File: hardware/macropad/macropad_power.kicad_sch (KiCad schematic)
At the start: 27 parts, among them J1 Conn_01x02, Q1 Q_PMOS, Q2 FS8205A, SW1 SW_SPDT, SW2 SW_SPDT, U1 TP4056-42-ESOP8, U2 DW01A, U3 RT8010AGQW, U4 LP2992IM5-3.3/NOPB

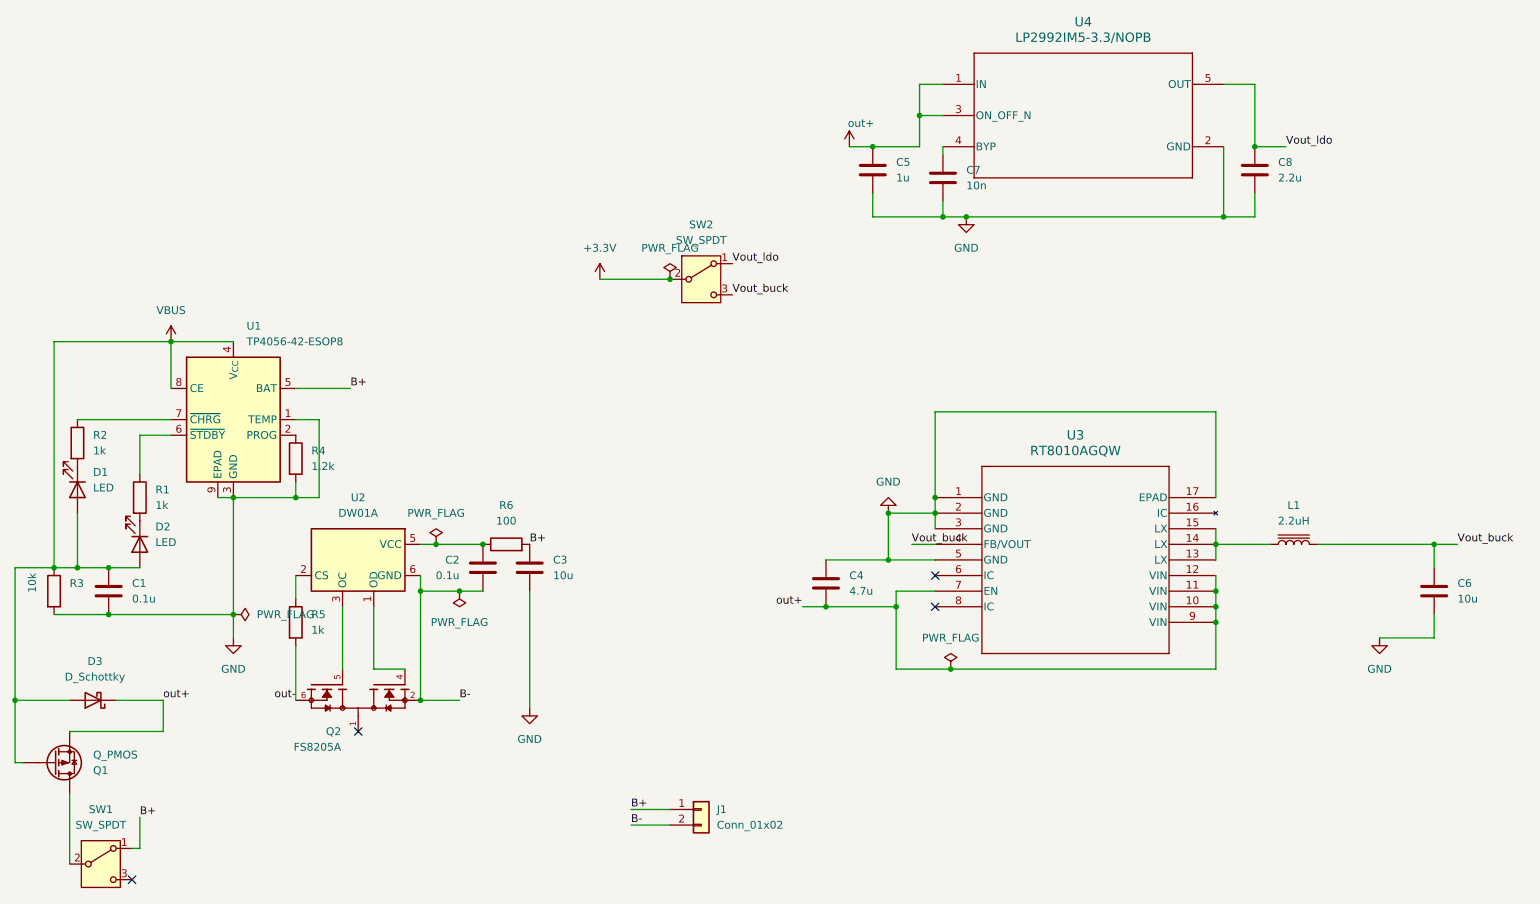
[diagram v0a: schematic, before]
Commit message: pcb macropad done
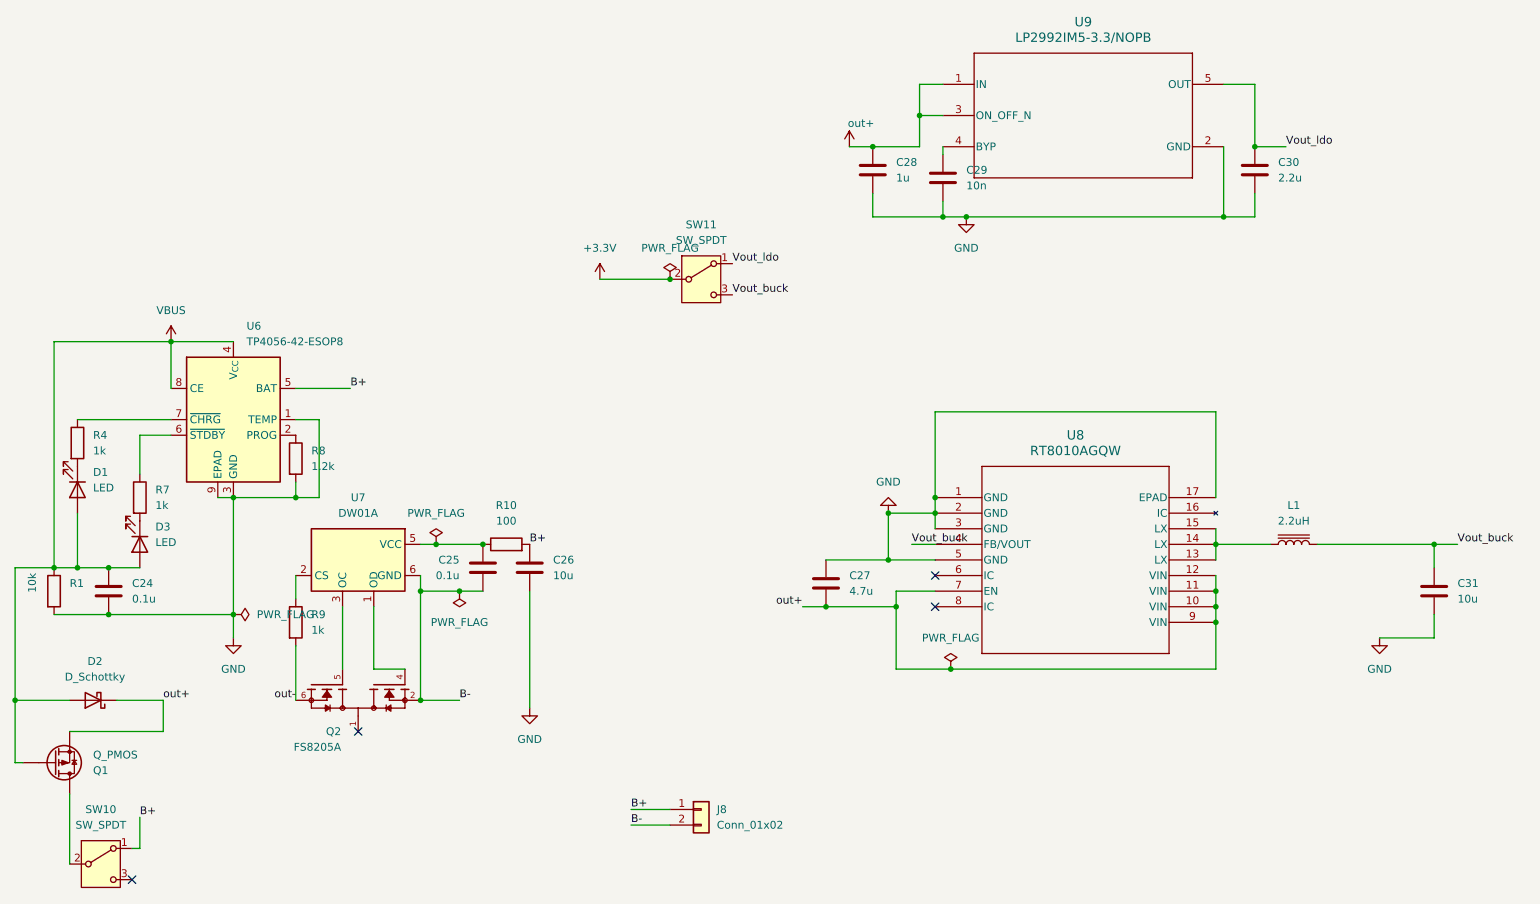
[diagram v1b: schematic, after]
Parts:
- renumbered C1 to C24, C2 to C25, C3 to C26, C4 to C27, C5 to C28, C7 to C29, C8 to C30, C6 to C31, D3 to D2, D2 to D3, J1 to J8, R3 to R1, R6 to R10, R2 to R4, R1 to R7, R4 to R8, R5 to R9, SW1 to SW10, SW2 to SW11, U1 to U6, U2 to U7, U3 to U8, U4 to U9

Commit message: routing
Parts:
- removed SW11: SW_SPDT, SS12F23L5:SS12F23L5 spdt, symbol Switch:SW_SPDT
- added J6: Conn_01x03_Socket, Connector_Hirose:Hirose_DF13-03P-1.25DSA_1x03_P1.25mm_Vertical, symbol Connector:Conn_01x03_Socket
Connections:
- net +3.3V: now also J6.2 (Pin_2)
- net Vout_buck: now also J6.1 (Pin_1)
- net Vout_ldo: now also J6.3 (Pin_3)
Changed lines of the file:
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@@
 	(paper "A3")
 	(junction
-		(at 196.85 86.36)
-		(diameter 0)
-		(color 0 0 0 0)
-	)
-	(junction
 		(at 285.75 129.54)
 		(diameter 0)
@@
 	)
 	(junction
+		(at 185.42 96.52)
+		(diameter 0)
+		(color 0 0 0 0)
+	)
+	(junction
 		(at 285.75 139.7)
 		(diameter 0)
@@
 	(wire
 		(pts
+			(xy 173.99 96.52) (xy 173.99 95.25)
+		)
+		(stroke
+			(width 0)
+			(type default)
+		)
+	)
+	(wire
+		(pts
 			(xy 106.68 154.94) (xy 114.3 154.94)
 		)
@@
 	(wire
 		(pts
+			(xy 185.42 96.52) (xy 185.42 95.25)
+		)
+		(stroke
+			(width 0)
+			(type default)
+		)
+	)
+	(wire
+		(pts
 			(xy 297.18 64.77) (xy 292.1 64.77)
 		)
@@
 	(wire
 		(pts
+			(xy 185.42 96.52) (xy 198.12 96.52)
+		)
+		(stroke
+			(width 0)
+			(type default)
+		)
+	)
+	(wire
+		(pts
 			(xy 156.21 137.16) (xy 156.21 134.62)
 		)
@@
 	(wire
 		(pts
-			(xy 185.42 86.36) (xy 196.85 86.36)
+			(xy 173.99 96.52) (xy 185.42 96.52)
 		)
 		(stroke
@@
 	)
 	(label "Vout_buck"
-		(at 207.01 88.9 0)
+		(at 198.12 93.98 180)
 		(effects
 			(font
 				(size 1.27 1.27)
 			)
-			(justify left bottom)
+			(justify right bottom)
 		)
 	)
@@
 	)
 	(label "Vout_ldo"
-		(at 207.01 83.82 0)
+		(at 198.12 99.06 180)
 		(effects
 			(font
 				(size 1.27 1.27)
 			)
-			(justify left bottom)
+			(justify right bottom)
 		)
 	)
@@
 	(symbol
 		(lib_id "power:PWR_FLAG")
-		(at 196.85 86.36 0)
+		(at 185.42 95.25 0)
 		(unit 1)
 		(exclude_from_sim no)
@@
 		(fields_autoplaced yes)
 		(property "Reference" "#FLG0104"
-			(at 196.85 84.455 0)
+			(at 185.42 93.345 0)
 			(effects
 				(font
@@
 		)
 		(property "Value" "PWR_FLAG"
-			(at 196.85 81.28 0)
+			(at 185.42 90.17 0)
 			(effects
 				(font
@@
 		)
 		(property "Footprint" ""
-			(at 196.85 86.36 0)
+			(at 185.42 95.25 0)
 			(effects
 				(font
@@
 		)
 		(property "Datasheet" "~"
-			(at 196.85 86.36 0)
+			(at 185.42 95.25 0)
 			(effects
 				(font
@@
 		)
 		(property "Description" "Special symbol for telling ERC where power comes from"
-			(at 196.85 86.36 0)
+			(at 185.42 95.25 0)
 			(effects
 				(font
@@
 	)
 	(symbol
+		(lib_id "Connector:Conn_01x03_Socket")
+		(at 203.2 96.52 0)
+		(unit 1)
+		(exclude_from_sim no)
+		(in_bom yes)
+		(on_board yes)
+		(dnp no)
+		(fields_autoplaced yes)
+		(property "Reference" "J6"
+			(at 204.47 95.2499 0)
+			(effects
+				(font
+					(size 1.27 1.27)
+				)
+				(justify left)
+			)
+		)
+		(property "Value" "Conn_01x03_Socket"
+			(at 204.47 97.7899 0)
+			(effects
+				(font
+					(size 1.27 1.27)
+				)
+				(justify left)
+			)
+		)
+		(property "Footprint" "Connector_Hirose:Hirose_DF13-03P-1.25DSA_1x03_P1.25mm_Vertical"
+			(at 203.2 96.52 0)
+			(effects
+				(font
+					(size 1.27 1.27)
+				)
+				(hide yes)
+			)
+		)
+		(property "Datasheet" "~"
+			(at 203.2 96.52 0)
+			(effects
+				(font
+					(size 1.27 1.27)
+				)
+				(hide yes)
+			)
+		)
+		(property "Description" "Generic connector, single row, 01x03, script generated"
+			(at 203.2 96.52 0)
+			(effects
+				(font
+					(size 1.27 1.27)
+				)
+				(hide yes)
+			)
+		)
+		(pin "3"
+		)
+		(pin "2"
+		)
+		(pin "1"
+		)
+		(instances
+			(project ""
+				(path "/228dc472-b306-4e5f-8dc5-2bf23eb4978d/5b38d27c-d7f4-4a8d-8a5e-966bba03fead"
+					(reference "J6")
+					(unit 1)
+				)
+			)
+		)
+	)
+	(symbol
 		(lib_id "power:GND")
 		(at 232.41 124.46 180)
@@
 	)
 	(symbol
-		(lib_id "Switch:SW_SPDT")
-		(at 201.93 86.36 0)
-		(unit 1)
-		(exclude_from_sim no)
-		(in_bom yes)
-		(on_board yes)
-		(dnp no)
-		(fields_autoplaced yes)
-		(property "Reference" "SW11"
-			(at 201.93 77.47 0)
-			(effects
-				(font
-					(size 1.27 1.27)
-				)
-			)
-		)
-		(property "Value" "SW_SPDT"
-			(at 201.93 80.01 0)
-			(effects
-				(font
-					(size 1.27 1.27)
-				)
-			)
-		)
-		(property "Footprint" "SS12F23L5:SS12F23L5 spdt"
-			(at 201.93 86.36 0)
-			(effects
-				(font
-					(size 1.27 1.27)
-				)
-				(hide yes)
-			)
-		)
-		(property "Datasheet" "~"
-			(at 201.93 93.98 0)
-			(effects
-				(font
-					(size 1.27 1.27)
-				)
-				(hide yes)
-			)
-		)
-		(property "Description" "Switch, single pole double throw"
-			(at 201.93 86.36 0)
-			(effects
-				(font
-					(size 1.27 1.27)
-				)
-				(hide yes)
-			)
-		)
-		(pin "3"
-		)
-		(pin "2"
-		)
-		(pin "1"
-		)
-		(instances
-			(project "macropad_power"
-				(path "/228dc472-b306-4e5f-8dc5-2bf23eb4978d"
-					(reference "SW2")
-					(unit 1)
-				)
-				(path "/228dc472-b306-4e5f-8dc5-2bf23eb4978d/5b38d27c-d7f4-4a8d-8a5e-966bba03fead"
-					(reference "SW11")
-					(unit 1)
-				)
-			)
-		)
-	)
-	(symbol
 		(lib_id "power:GND")
 		(at 312.42 144.78 0)
@@
 	(symbol
 		(lib_id "power:+3.3V")
-		(at 185.42 86.36 0)
+		(at 173.99 95.25 0)
 		(unit 1)
 		(exclude_from_sim no)
@@
 		(fields_autoplaced yes)
 		(property "Reference" "#PWR0103"
-			(at 185.42 90.17 0)
+			(at 173.99 99.06 0)
 			(effects
 				(font
@@
 		)
 		(property "Value" "+3.3V"
-			(at 185.42 81.28 0)
+			(at 173.99 90.17 0)
 			(effects
 				(font
@@
 		)
 		(property "Footprint" ""
-			(at 185.42 86.36 0)
+			(at 173.99 95.25 0)
 			(effects
 				(font
@@
 		)
 		(property "Datasheet" ""
-			(at 185.42 86.36 0)
+			(at 173.99 95.25 0)
 			(effects
 				(font
@@
 		)
 		(property "Description" "Power symbol creates a global label with name \"+3.3V\""
-			(at 185.42 86.36 0)
+			(at 173.99 95.25 0)
 			(effects
 				(font

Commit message: routing phase 2
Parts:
- removed U8: RT8010AGQW, RT8010:WQFN16_RT8010_RIT, symbol RT8010:RT8010AGQW
- added U10: ~, RT8010:WDFN-6L, symbol rt8010:rt8010_wdfn
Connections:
- net GND: now also U10.5 (GND), U10.7 (GND)
- net Vout_buck: now also U10.6 (FB/VOUT)
- net out+: now also U10.2 (EN), U10.3 (VIN)
- net at L1.1: now also U10.4 (SW)
- no-connect marks 4 -> 3
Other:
- moved on the sheet: C27, C31, L1

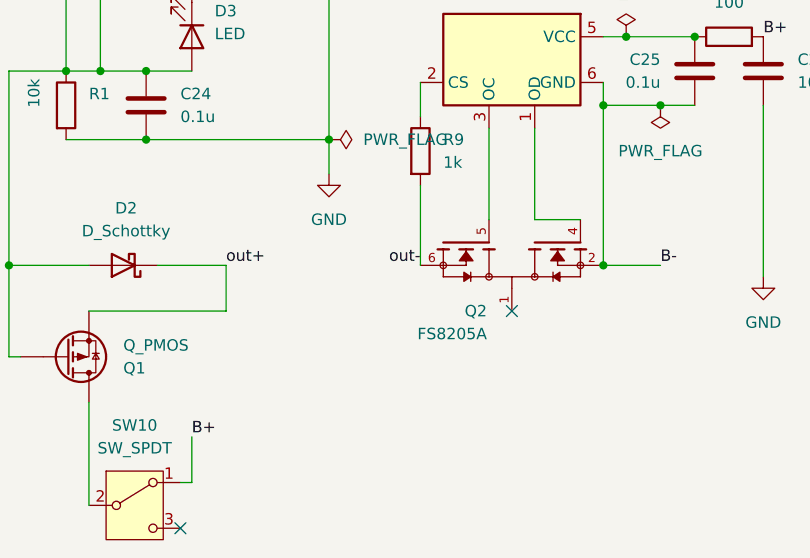
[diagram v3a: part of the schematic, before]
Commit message: updated dongle
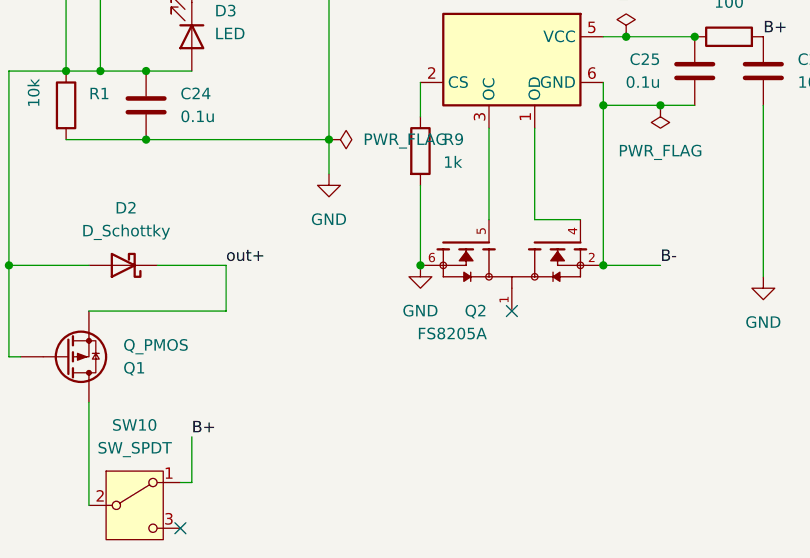
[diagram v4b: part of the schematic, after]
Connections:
- net out- is gone; now on net GND: Q2.6, Q2.7, R9.2
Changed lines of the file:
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@@
 	(paper "A3")
 	(junction
+		(at 135.89 154.94)
+		(diameter 0)
+		(color 0 0 0 0)
+	)
+	(junction
 		(at 115.57 96.52)
 		(diameter 0)
@@
 		)
 	)
-	(label "out-"
-		(at 135.89 154.94 180)
-		(effects
-			(font
-				(size 1.27 1.27)
-			)
-			(justify right bottom)
-		)
-	)
 	(label "Vout_buck"
 		(at 304.8 129.54 0)
@@
 					(unit 1)
 				)
+			)
+		)
+	)
+	(symbol
+		(lib_id "power:GND")
+		(at 135.89 154.94 0)
+		(unit 1)
+		(exclude_from_sim no)
+		(in_bom yes)
+		(on_board yes)
+		(dnp no)
+		(fields_autoplaced yes)
+		(property "Reference" "#PWR016"
+			(at 135.89 161.29 0)
+			(effects
+				(font
+					(size 1.27 1.27)
+				)
+				(hide yes)
+			)
+		)
+		(property "Value" "GND"
+			(at 135.89 160.02 0)
+			(effects
+				(font
+					(size 1.27 1.27)
+				)
+			)
+		)
+		(property "Footprint" ""
+			(at 135.89 154.94 0)
+			(effects
+				(font
+					(size 1.27 1.27)
+				)
+				(hide yes)
+			)
+		)
+		(property "Datasheet" ""
+			(at 135.89 154.94 0)
+			(effects
+				(font
+					(size 1.27 1.27)
+				)
+				(hide yes)
+			)
+		)
+		(property "Description" "Power symbol creates a global label with name \"GND\" , ground"
+			(at 135.89 154.94 0)
+			(effects
+				(font
+					(size 1.27 1.27)
+				)
+				(hide yes)
+			)
+		)
+		(pin "1"
+		)
+		(instances
+			(project "macropad"
+				(path "/228dc472-b306-4e5f-8dc5-2bf23eb4978d/5b38d27c-d7f4-4a8d-8a5e-966bba03fead"
+					(reference "#PWR016")
+					(unit 1)
+				)

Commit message: fab outputs
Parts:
- C24, C25: value 0.1u -> 100n
- J6: now not fitted

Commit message: proper fab outs
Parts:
- C24: MPN (none) -> AC0603JRX7R9BB104
- C26: MPN (none) -> GRT21BR61C106KE01L
- C27: MPN (none) -> GRM188Z71C475KE21D
- C30: MPN (none) -> TMK107BBJ225KAHT
- D2: MPN (none) -> SS34
- D3: MPN (none) -> 17-21SURC/S530-A3/4T
- J8, SW10: now not fitted
- L1: MPN (none) -> CDRH104R 2.2uH
- Q1: MPN (none) -> SI2305CDS-T1-GE3
- Q2: MPN (none) -> FS8205A
- R10: MPN (none) -> AC0201FR-07100RL
- R8: MPN (none) -> AC0603FR-071K2L
- R9: MPN (none) -> AC0603FR-071KL
- U10: MPN (none) -> RT8010-33GQW
- U6: MPN (none) -> TP4056
- U7: MPN (none) -> DW01A
- U9: MPN (none) -> LP2992IM5-3.3/NOPB
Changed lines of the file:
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@@
+			)
+		)
+		(property "MPN" "AC0603FR-071KL"
+			(at 135.89 142.24 0)
+			(effects
+				(font
+					(size 1.27 1.27)
+				)
+				(hide yes)
 			)
 		)
@@
 			)
 		)
+		(property "MPN" "CDRH104R 2.2uH"
+			(at 285.75 129.54 90)
+			(effects
+				(font
+					(size 1.27 1.27)
+				)
+				(hide yes)
+			)
+		)
 		(pin "1"
 		)
@@
 			)
 		)
+		(property "MPN" "TMK107BBJ225KAHT"
+			(at 292.1 68.58 0)
+			(effects
+				(font
+					(size 1.27 1.27)
+				)
+				(hide yes)
+			)
+		)
 		(pin "2"
 		)
@@
 		)
 		(property "Description" "Resistor"
+			(at 135.89 115.57 0)
+			(effects
+				(font
+					(size 1.27 1.27)
+				)
+				(hide yes)
+			)
+		)
+		(property "MPN" "AC0603FR-071K2L"
 			(at 135.89 115.57 0)
 			(effects
@@
 			)
 		)
+		(property "MPN" "SI2305CDS-T1-GE3"
+			(at 96.52 165.1 0)
+			(effects
+				(font
+					(size 1.27 1.27)
+				)
+				(hide yes)
+			)
+		)
 		(pin "3"
 		)
@@
 		(in_bom yes)
 		(on_board yes)
-		(dnp no)
+		(dnp yes)
 		(fields_autoplaced yes)
 		(property "Reference" "SW10"
@@
 		(in_bom yes)
 		(on_board yes)
-		(dnp no)
+		(dnp yes)
 		(fields_autoplaced yes)
 		(property "Reference" "J8"
@@
 			)
 		)
+		(property "MPN" "LP2992IM5-3.3/NOPB"
+			(at 264.16 59.69 0)
+			(effects
+				(font
+					(size 1.27 1.27)
+				)
+				(hide yes)
+			)
+		)
 		(pin "3"
 		)
@@
 			)
 		)
+		(property "MPN" "AC0201FR-07100RL"
+			(at 170.18 129.54 90)
+			(effects
+				(font
+					(size 1.27 1.27)
+				)
+				(hide yes)
+			)
+		)
 		(pin "1"
 		)
@@
 			)
 		)
+		(property "MPN" "RT8010-33GQW"
+			(at 260.35 120.65 0)
+			(effects
+				(font
+					(size 1.27 1.27)
+				)
+				(hide yes)
+			)
+		)
 		(pin "5"
 		)
@@
 			)
 		)
+		(property "MPN" "17-21SURC/S530-A3/4T"
+			(at 110.49 129.54 90)
+			(effects
+				(font
+					(size 1.27 1.27)
+				)
+				(hide yes)
+			)
+		)
 		(pin "1"
 		)
@@
 		)
 		(property "Description" "Schottky diode"
+			(at 102.87 154.94 0)
+			(effects
+				(font
+					(size 1.27 1.27)
+				)
+				(hide yes)
+			)
+		)
+		(property "MPN" "SS34"
 			(at 102.87 154.94 0)
 			(effects
@@
 			)
 		)
+		(property "MPN" "FS8205A"
+			(at 146.05 154.94 90)
+			(effects
+				(font
+					(size 1.27 1.27)
+				)
+				(hide yes)
+			)
+		)
 		(pin "1"
 		)
@@
 		)
 		(property "Description" "Unpolarized capacitor"
+			(at 173.99 133.35 0)
+			(effects
+				(font
+					(size 1.27 1.27)
+				)
+				(hide yes)
+			)
+		)
+		(property "MPN" "GRT21BR61C106KE01L"
 			(at 173.99 133.35 0)
 			(effects
@@
 			)
 		)
+		(property "MPN" "DW01A"
+			(at 146.05 132.08 0)
+			(effects
+				(font
+					(size 1.27 1.27)
+				)
+				(hide yes)
+			)
+		)
 		(pin "5"
 		)
@@
 			)
 		)
+		(property "MPN" "GRM188Z71C475KE21D"
+			(at 234.95 125.73 0)
+			(effects
+				(font
+					(size 1.27 1.27)
+				)
+				(hide yes)
+			)
+		)
 		(pin "2"
 		)
@@
 			)
 		)
+		(property "MPN" "TP4056"
+			(at 125.73 109.22 0)
+			(effects
+				(font
+					(size 1.27 1.27)
+				)
+				(hide yes)
+			)
+		)
 		(pin "2"
 		)
@@
 			(at 105.41 137.16 0)
 			(effects
+				(font
+					(size 1.27 1.27)
+				)
+				(hide yes)
+			)
+		)
+		(property "MPN" "AC0603JRX7R9BB104"
+			(at 105.41 137.16 0)
+			(effects

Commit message: fixed technical queries
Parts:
- R10: footprint Resistor_SMD:R_0603_1608Metric -> Resistor_SMD:R_0201_0603Metric
- U10: value ~ -> RT8010
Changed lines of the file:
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@@
 			)
 		)
-		(property "Footprint" "Resistor_SMD:R_0603_1608Metric"
+		(property "Footprint" "Resistor_SMD:R_0201_0603Metric"
 			(at 170.18 131.318 90)
 			(effects
@@
 			)
 		)
-		(property "Value" "~"
+		(property "Value" "RT8010"
 			(at 260.35 120.65 0)
 			(effects
